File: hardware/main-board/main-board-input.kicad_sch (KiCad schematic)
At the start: 37 parts, among them J4 Conn_01x02, SW1 SW_Push_Long, SW10 SW_Push_LED, SW11 Rotary_Encoder_Switch, SW2 SW_Push_Long, SW3 SW_Push, SW4 SW_Push, SW5 SW_Push, SW6 SW_Push, SW7 SW_Push_LED, SW8 SW_Push_LED, SW9 SW_Push_LED, U7 TCA8418, U8 STP16CPC26

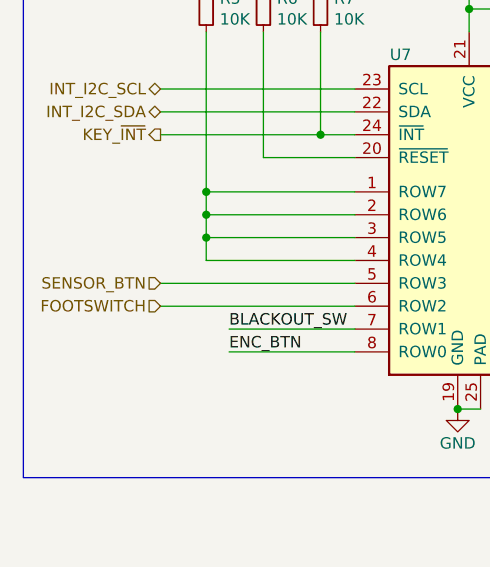
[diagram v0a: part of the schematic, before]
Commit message: Schematic updates for power regulator filtering and meter interface
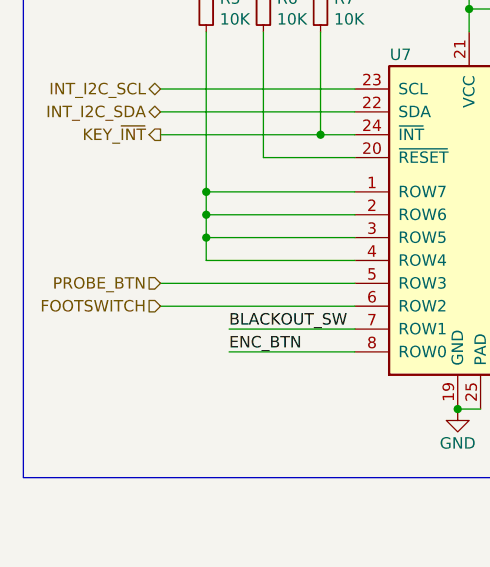
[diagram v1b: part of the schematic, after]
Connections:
- net SENSOR_BTN renamed PROBE_BTN
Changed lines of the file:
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@@
     (effects (font (size 1.27 1.27) italic) (justify right))
   )
-  (hierarchical_label "SENSOR_BTN" (shape input) (at 31.75 120.65 180) (fields_autoplaced)
+  (hierarchical_label "PROBE_BTN" (shape input) (at 31.75 120.65 180) (fields_autoplaced)
     (effects (font (size 1.27 1.27)) (justify right))
   )

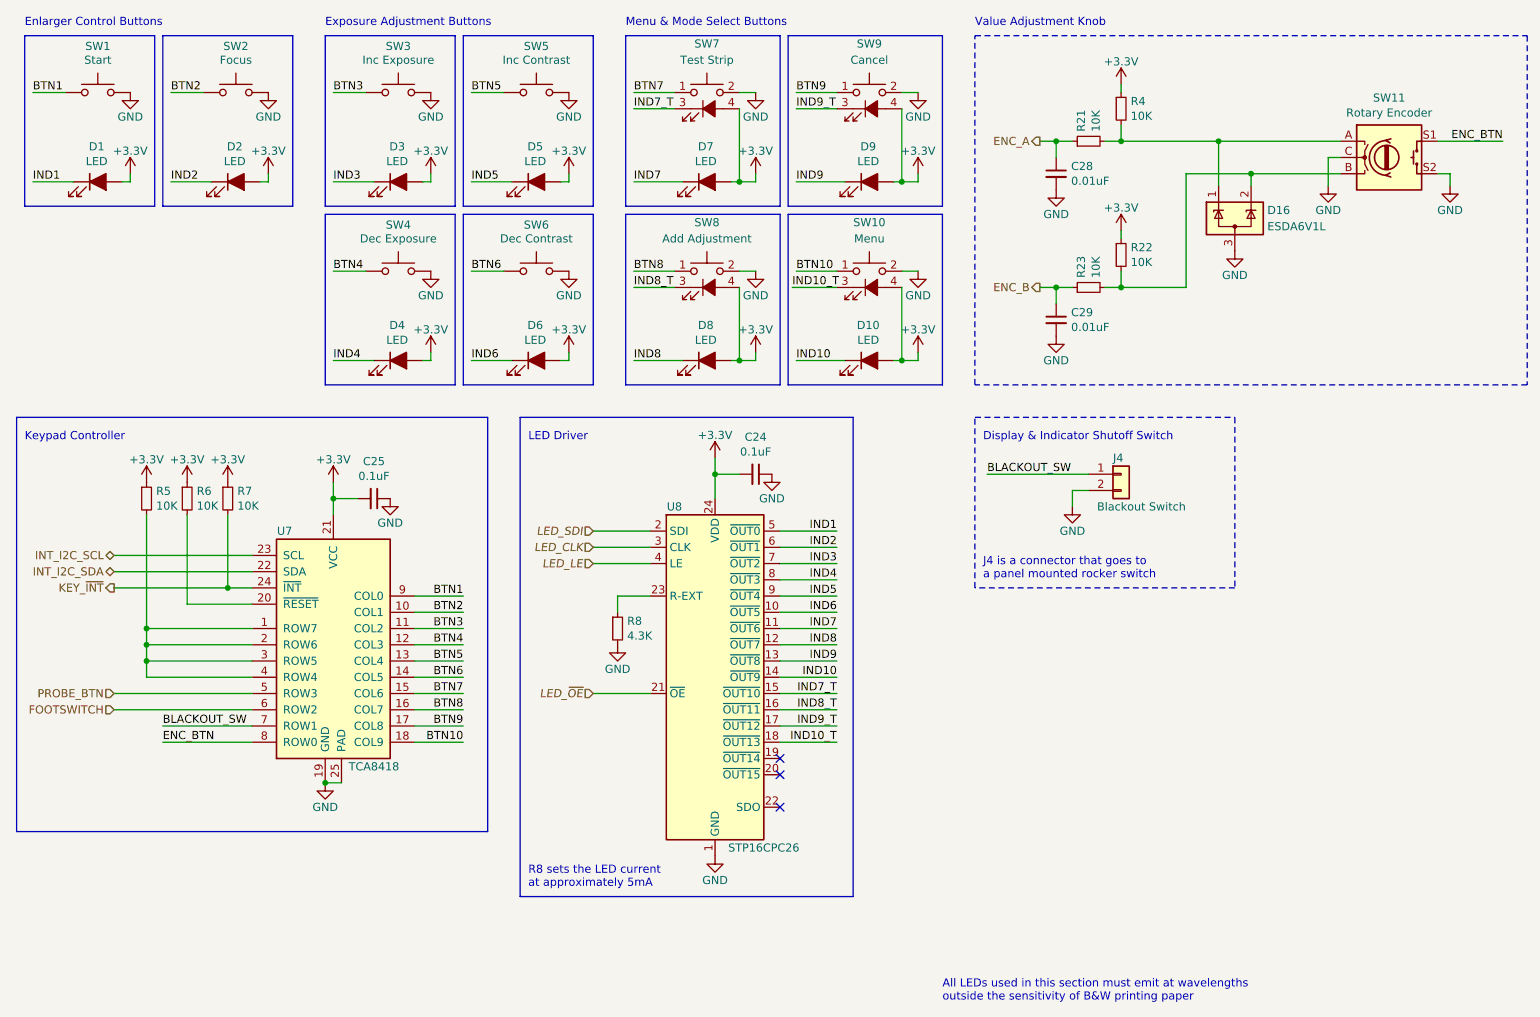
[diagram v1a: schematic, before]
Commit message: Renumbered reference designators on main board
This board has changed so much that its better to take this hit than
have the numbers appear random during board assembly.
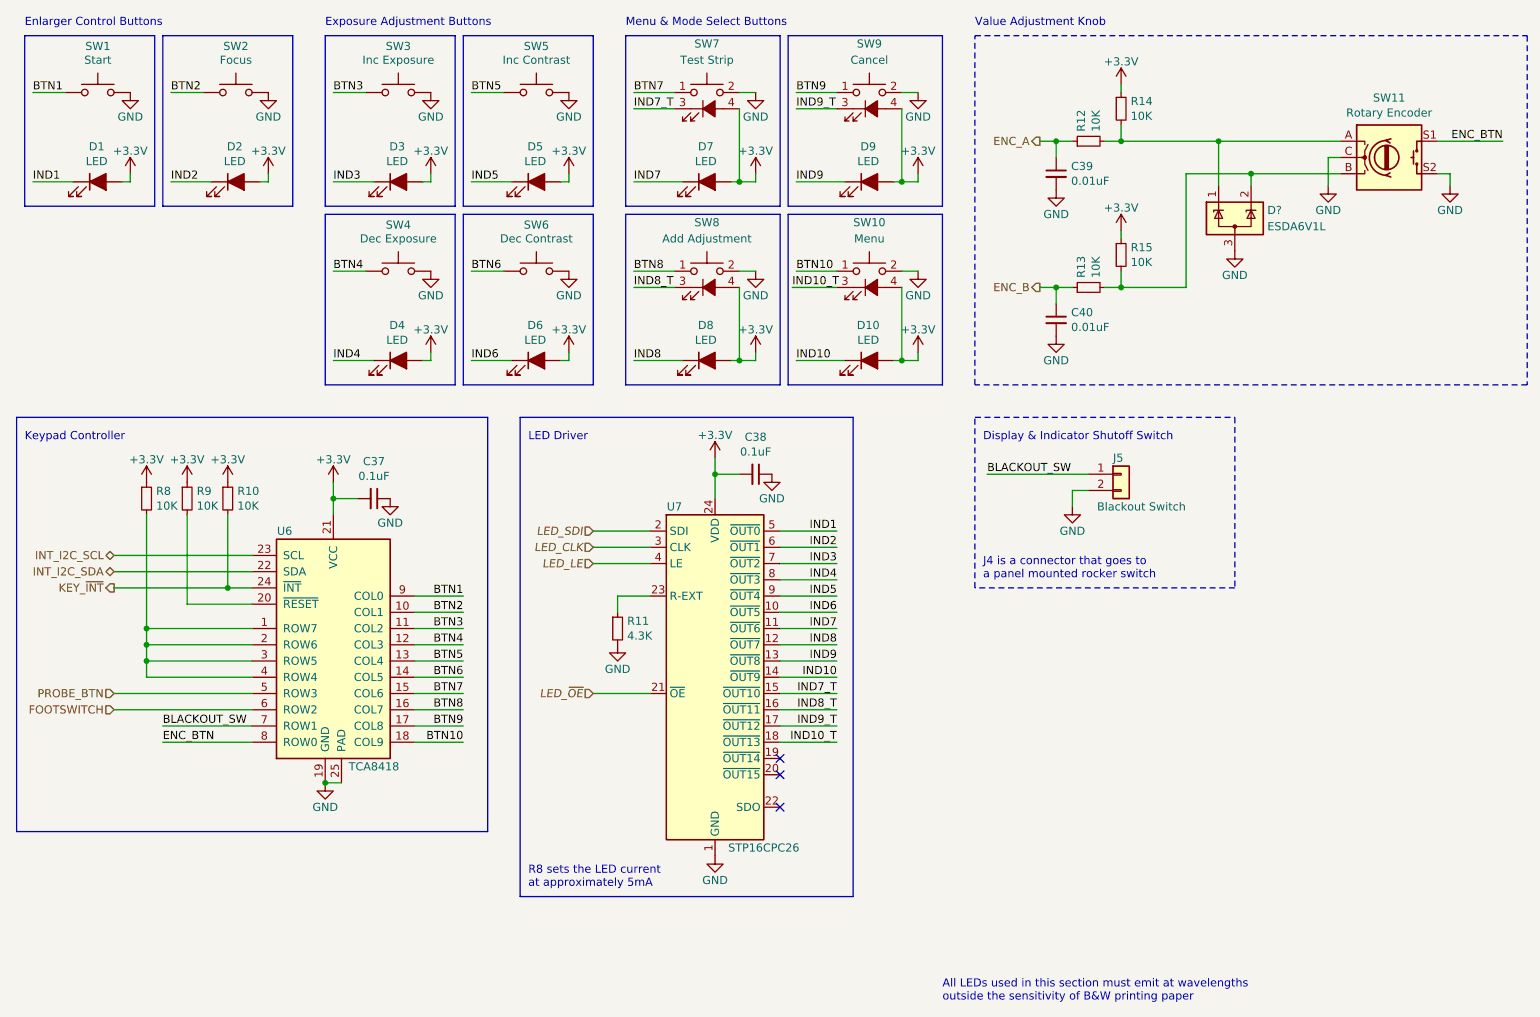
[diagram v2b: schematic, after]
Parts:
- renumbered C25 to C37, C24 to C38, C28 to C39, C29 to C40, D16 to D?, J4 to J5, R7 to R10, R8 to R11, R21 to R12, R23 to R13, R4 to R14, R22 to R15, R5 to R8, R6 to R9, U7 to U6, U8 to U7

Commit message: Change rotary encoder part
The new part is a bit taller, and should work better mechanically.

Refs #42
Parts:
- SW11: footprint lib_fp:RotaryEncoder_CUI_ACZ11BR1E-Switch_Vertical_H15mm -> lib_fp:RotaryEncoder_Bourns_PEC11L-Switch_Vertical_H20mm; Manufacturer CUI Devices -> Bourns Inc.; Manufacturer PN ACZ11BR1E-15FD1-20C -> PEC11L-4120F-S0020; Supplier Digi-Key -> Mouser; Supplier PN 102-1767-ND -> 652-PEC11L4120FS0020
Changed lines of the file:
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@@
       (effects (font (size 1.27 1.27)) hide)
     )
-    (property "Footprint" "lib_fp:RotaryEncoder_CUI_ACZ11BR1E-Switch_Vertical_H15mm" (at 227.33 32.766 0)
+    (property "Footprint" "lib_fp:RotaryEncoder_Bourns_PEC11L-Switch_Vertical_H20mm" (at 227.33 32.766 0)
       (effects (font (size 1.27 1.27)) hide)
     )
-    (property "Datasheet" "https://www.cuidevices.com/product/resource/digikeypdf/acz11.pdf" (at 231.14 30.226 0)
+    (property "Datasheet" "https://www.bourns.com/docs/Product-Datasheets/PEC11L.pdf" (at 231.14 30.226 0)
       (effects (font (size 1.27 1.27)) hide)
     )
@@
       (effects (font (size 1.27 1.27)))
     )
-    (property "Description" "ROTARY ENCODER INCREMENT 20PPR" (at 231.14 36.83 0)
+    (property "Description" "ROTARY ENCODER MECHANICAL 20PPR" (at 231.14 36.83 0)
       (effects (font (size 1.27 1.27)) hide)
     )
-    (property "Manufacturer" "CUI Devices" (at 231.14 36.83 0)
+    (property "Manufacturer" "Bourns Inc." (at 231.14 36.83 0)
       (effects (font (size 1.27 1.27)) hide)
     )
-    (property "Manufacturer PN" "ACZ11BR1E-15FD1-20C" (at 231.14 36.83 0)
+    (property "Manufacturer PN" "PEC11L-4120F-S0020" (at 231.14 36.83 0)
       (effects (font (size 1.27 1.27)) hide)
     )
-    (property "Supplier" "Digi-Key" (at 231.14 36.83 0)
+    (property "Supplier" "Mouser" (at 231.14 36.83 0)
       (effects (font (size 1.27 1.27)) hide)
     )
-    (property "Supplier PN" "102-1767-ND" (at 231.14 36.83 0)
+    (property "Supplier PN" "652-PEC11L4120FS0020" (at 231.14 36.83 0)
       (effects (font (size 1.27 1.27)) hide)
     )

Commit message: Various BOM tweaks
Merged all 0.01uF 0603 capacitors to use the same 50V rated part, to
avoid needing separate components for power and non-power use cases.

Switched panel LED current resistor tolerance from 5% to 1% for better
unit-to-unit consistency.
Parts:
- C39, C40: Manufacturer PN CL10B103KA8NNNC -> CL10B103KB8NNNC; Supplier PN 1276-1132-1-ND -> 1276-1009-1-ND
- R11: Manufacturer PN CRCW06034K30JNEA -> CRCW06034K30FKEA; Supplier PN 541-4.3KGCT-ND -> 541-4.30KHCT-ND
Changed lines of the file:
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@@
       (effects (font (size 1.27 1.27)) hide)
     )
-    (property "Description" "RES SMD 4.3K OHM 5% 1/10W 0603" (at 110.49 110.49 0)
+    (property "Description" "RES SMD 4.3K OHM 1% 1/10W 0603" (at 110.49 110.49 0)
       (effects (font (size 1.27 1.27)) hide)
     )
@@
       (effects (font (size 1.27 1.27)) hide)
     )
-    (property "Manufacturer PN" "CRCW06034K30JNEA" (at 110.49 110.49 0)
+    (property "Manufacturer PN" "CRCW06034K30FKEA" (at 110.49 110.49 0)
       (effects (font (size 1.27 1.27)) hide)
     )
@@
       (effects (font (size 1.27 1.27)) hide)
     )
-    (property "Supplier PN" "541-4.3KGCT-ND" (at 110.49 110.49 0)
+    (property "Supplier PN" "541-4.30KHCT-ND" (at 110.49 110.49 0)
       (effects (font (size 1.27 1.27)) hide)
     )
@@
       (effects (font (size 1.27 1.27)) hide)
     )
-    (property "Datasheet" "https://media.digikey.com/pdf/Data%20Sheets/Samsung%20PDFs/CL_Series_MLCC_ds.pdf" (at 179.07 39.37 0)
-      (effects (font (size 1.27 1.27)) hide)
-    )
-    (property "Description" "CAP CER 10000PF 25V X7R 0603" (at 179.07 39.37 0)
+    (property "Datasheet" "https://media.digikey.com/pdf/Data%20Sheets/Samsung%20PDFs/CL10B103KB8NNNC_Spec.pdf" (at 179.07 39.37 0)
+      (effects (font (size 1.27 1.27)) hide)
+    )
+    (property "Description" "CAP CER 10000PF 50V X7R 0603" (at 179.07 39.37 0)
       (effects (font (size 1.27 1.27)) hide)
     )
@@
       (effects (font (size 1.27 1.27)) hide)
     )
-    (property "Manufacturer PN" "CL10B103KA8NNNC" (at 179.07 39.37 0)
+    (property "Manufacturer PN" "CL10B103KB8NNNC" (at 179.07 39.37 0)
       (effects (font (size 1.27 1.27)) hide)
     )
@@
       (effects (font (size 1.27 1.27)) hide)
     )
-    (property "Supplier PN" "1276-1132-1-ND" (at 179.07 39.37 0)
+    (property "Supplier PN" "1276-1009-1-ND" (at 179.07 39.37 0)
       (effects (font (size 1.27 1.27)) hide)
     )
@@
       (effects (font (size 1.27 1.27)) hide)
     )
-    (property "Datasheet" "https://media.digikey.com/pdf/Data%20Sheets/Samsung%20PDFs/CL_Series_MLCC_ds.pdf" (at 179.07 62.23 0)
-      (effects (font (size 1.27 1.27)) hide)
-    )
-    (property "Description" "CAP CER 10000PF 25V X7R 0603" (at 179.07 62.23 0)
+    (property "Datasheet" "https://media.digikey.com/pdf/Data%20Sheets/Samsung%20PDFs/CL10B103KB8NNNC_Spec.pdf" (at 179.07 62.23 0)
+      (effects (font (size 1.27 1.27)) hide)
+    )
+    (property "Description" "CAP CER 10000PF 50V X7R 0603" (at 179.07 62.23 0)
       (effects (font (size 1.27 1.27)) hide)
     )
@@
       (effects (font (size 1.27 1.27)) hide)
     )
-    (property "Manufacturer PN" "CL10B103KA8NNNC" (at 179.07 62.23 0)
+    (property "Manufacturer PN" "CL10B103KB8NNNC" (at 179.07 62.23 0)
       (effects (font (size 1.27 1.27)) hide)
     )
@@
       (effects (font (size 1.27 1.27)) hide)
     )
-    (property "Supplier PN" "1276-1132-1-ND" (at 179.07 62.23 0)
-      (effects (font (size 1.27 1.27)) hide)
-    )
+    (property "Supplier PN" "1276-1009-1-ND" (at 179.07 62.23 0)
+      (effects (font (size 1.27 1.27)) hide)
+    )
